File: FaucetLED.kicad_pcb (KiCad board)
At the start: 2 copper layers, 34.5 x 28.4 mm, 43 parts, among them P1 CONN_01X03, P2 CONN_01X02, P4 CONN_01X03, P5 CONN_01X02, P6 CONN_01X01, Q1 BSS138, Q2 BSS138, Q3 BSS138, U1 TLV70033DDC, U2 STM32L052KxTx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

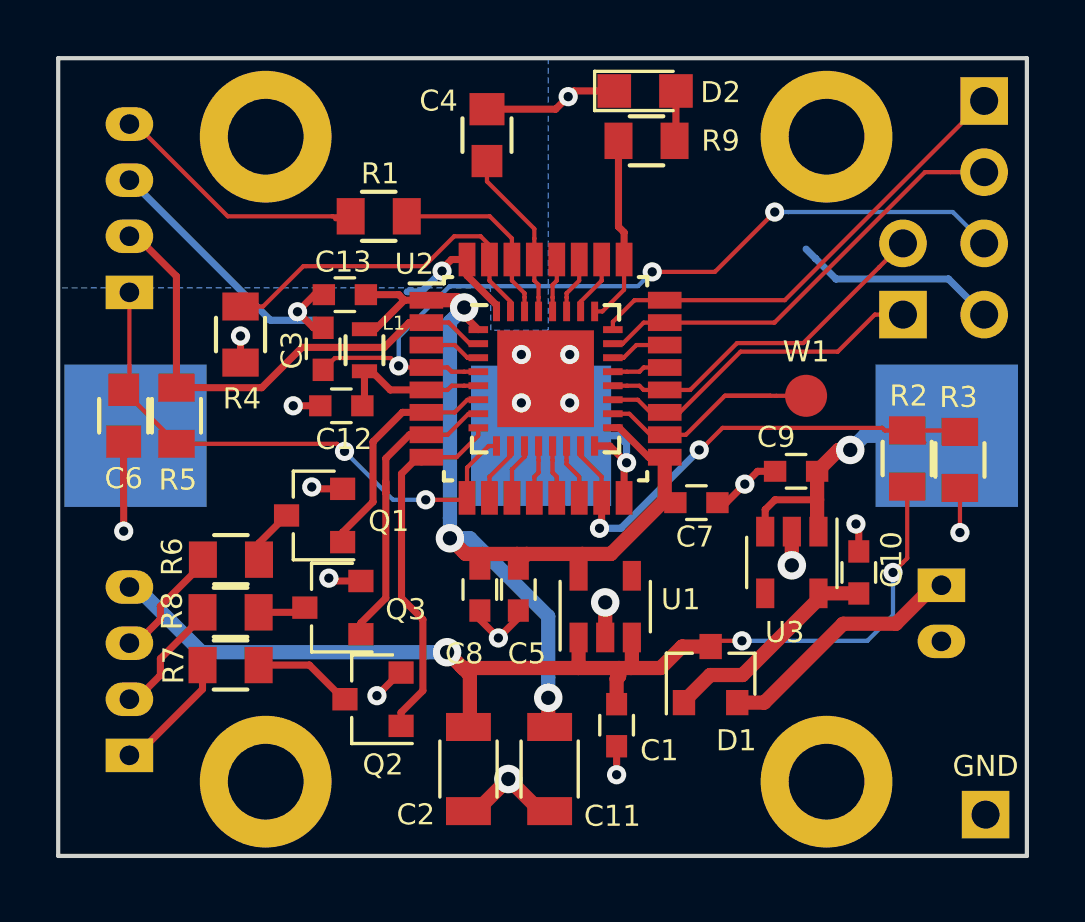
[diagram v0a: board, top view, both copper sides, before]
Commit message: Move 100uF cap to battery input.
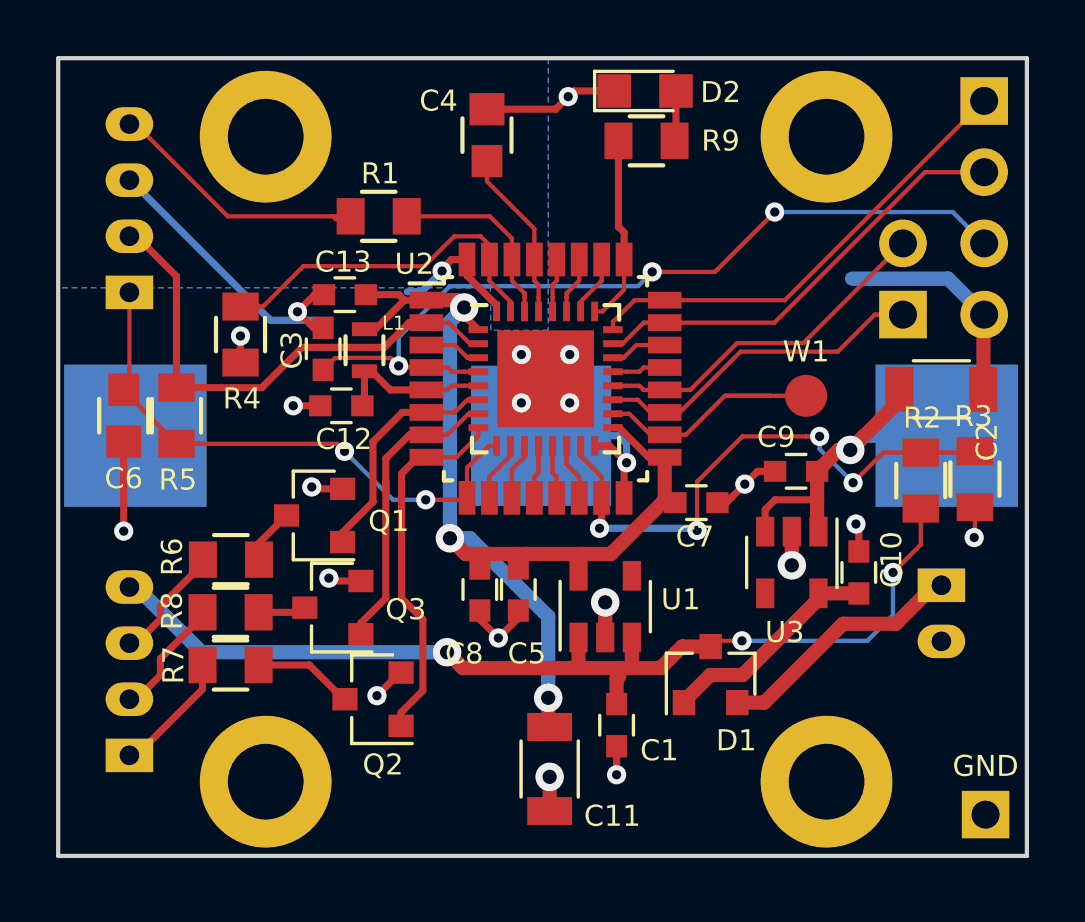
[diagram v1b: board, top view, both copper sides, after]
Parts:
- moved C2 21.6 mm to (133.1, 88.0), turned to 0 degrees
- moved R2 0.92 mm to (132.4, 91.3)
- moved R3 0.87 mm to (134.3, 91.2)
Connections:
- C2 pad 1: +BATT -> Net-(BT1-Pad1)
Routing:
- net Net-(BT1-Pad1): track 10.4 -> 13.3 mm
- net GND: track 65.2 -> 62.7 mm
- net /BATT_2: track 18.6 -> 20.5 mm, vias 2 -> 4
- net +BATT: track 39.9 -> 37.9 mm

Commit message: Move BATT_2 sense R's closer to ADC input.
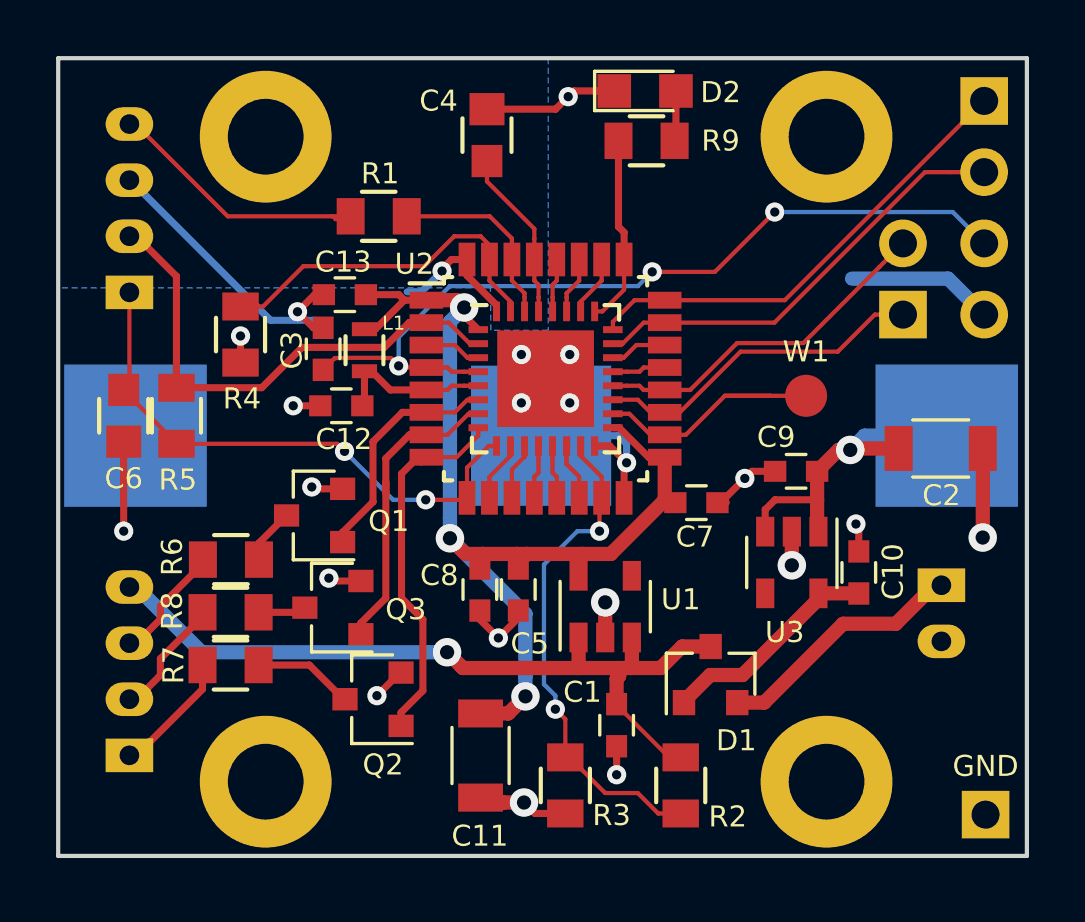
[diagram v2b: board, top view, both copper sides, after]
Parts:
- moved R3 18.2 mm to (119.7, 102.1)
- moved R2 13.8 mm to (123.8, 102.1), turned to 270 degrees
- moved C11 2.51 mm to (116.7, 101.1)
- moved C2 2.11 mm to (133.1, 90.1)
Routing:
- net +BATT: track 37.9 -> 29.4 mm, vias 3 -> 1
- net /BATT_2: track 20.5 -> 18.0 mm, vias 4 -> 2
- net GND: track 62.7 -> 64.5 mm
- net Net-(BT1-Pad1): track 13.3 -> 12.2 mm

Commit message: Add footprint for another bulk cap C14 on +BATT.
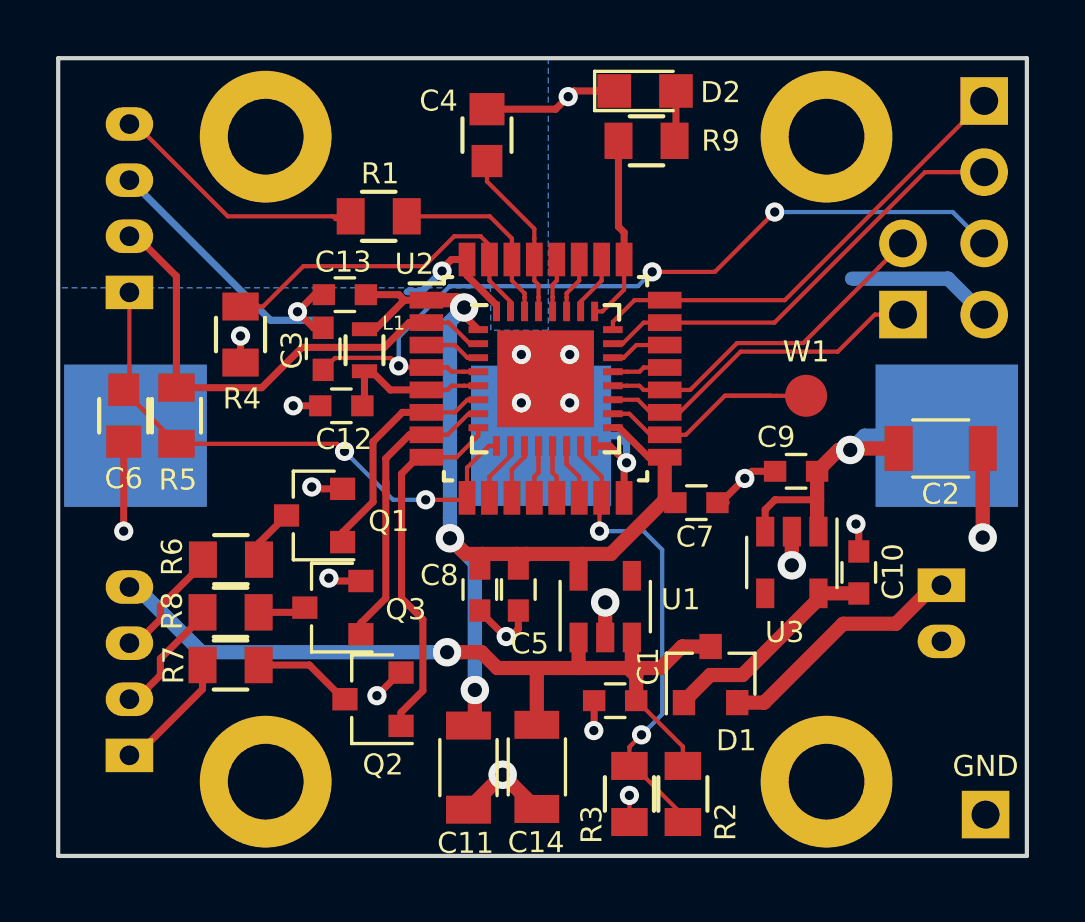
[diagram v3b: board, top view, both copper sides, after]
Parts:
- added C14: 100u, Capacitors_SMD:C_1206, F.Cu at (118.7, 101.5)
- moved R3 2.31 mm to (122.0, 102.4)
- moved C1 0.88 mm to (121.5, 99.1), turned to 180 degrees
- moved C11 0.61 mm to (116.2, 101.5)
- moved R2 0.31 mm to (123.9, 102.4)
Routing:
- net +BATT: track 29.4 -> 31.3 mm
- net +3V3: track 38.6 -> 37.1 mm
- net GND: track 64.5 -> 65.9 mm, vias 22 -> 23
- net /BATT_2: track 18.0 -> 17.0 mm

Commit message: Change C2 and C14 to 1210 package for lower leakage.
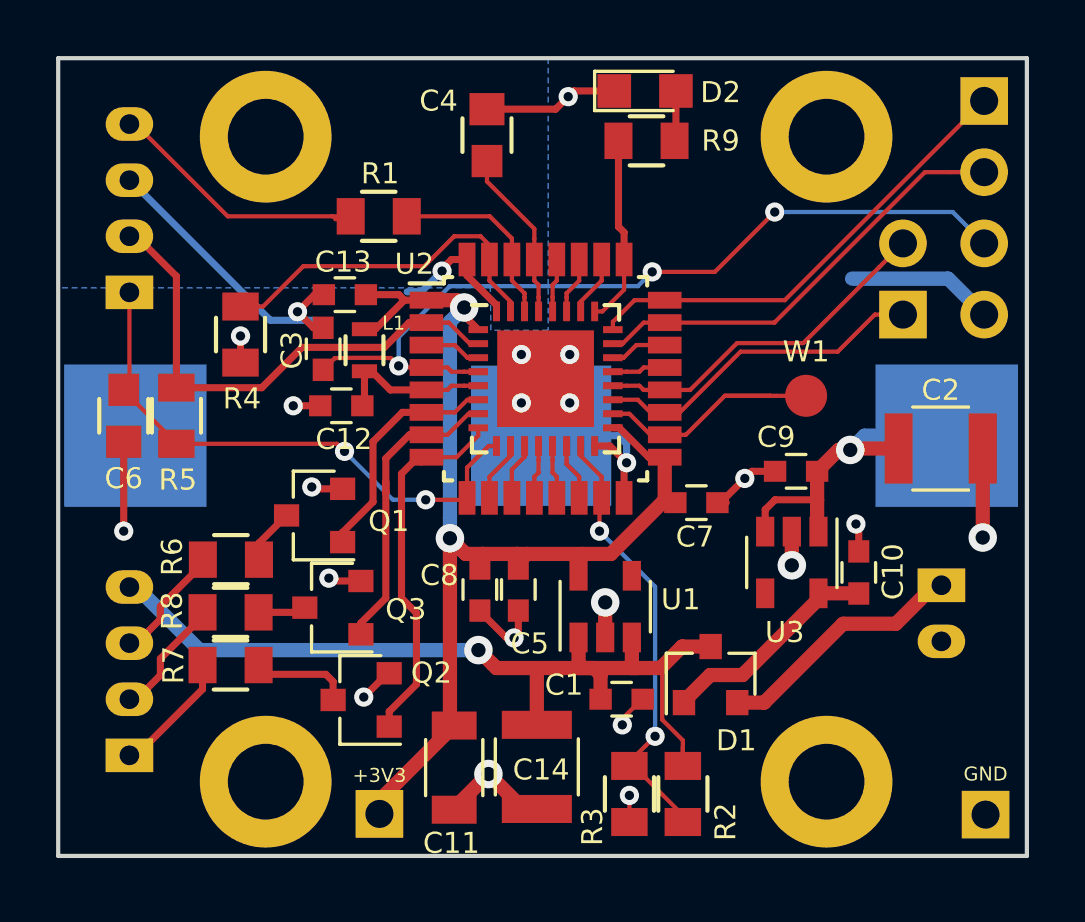
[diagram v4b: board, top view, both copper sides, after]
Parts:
- added P3: CONN_01X01, Pin_Headers:Pin_Header_Straight_1x01_Pitch2.54mm, F.Cu at (113.1, 103.1)
- C14, C2: footprint Capacitors_SMD:C_1206 -> Capacitors_SMD:C_1210
- moved C11 0.51 mm to (115.7, 101.5)
- moved Q2 0.42 mm to (112.4, 99.1)
- moved C1 0.23 mm to (121.7, 99.1), turned to 0 degrees
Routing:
- net +3V3: track 37.1 -> 41.0 mm, vias 3 -> 2
- net +BATT: track 31.3 -> 33.5 mm
- net /BATT_2: track 17.0 -> 15.8 mm
- net GND: track 65.9 -> 66.8 mm
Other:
- board text added: "+3V3"

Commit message: Slight move of C5 closer to 3.3V LDO.
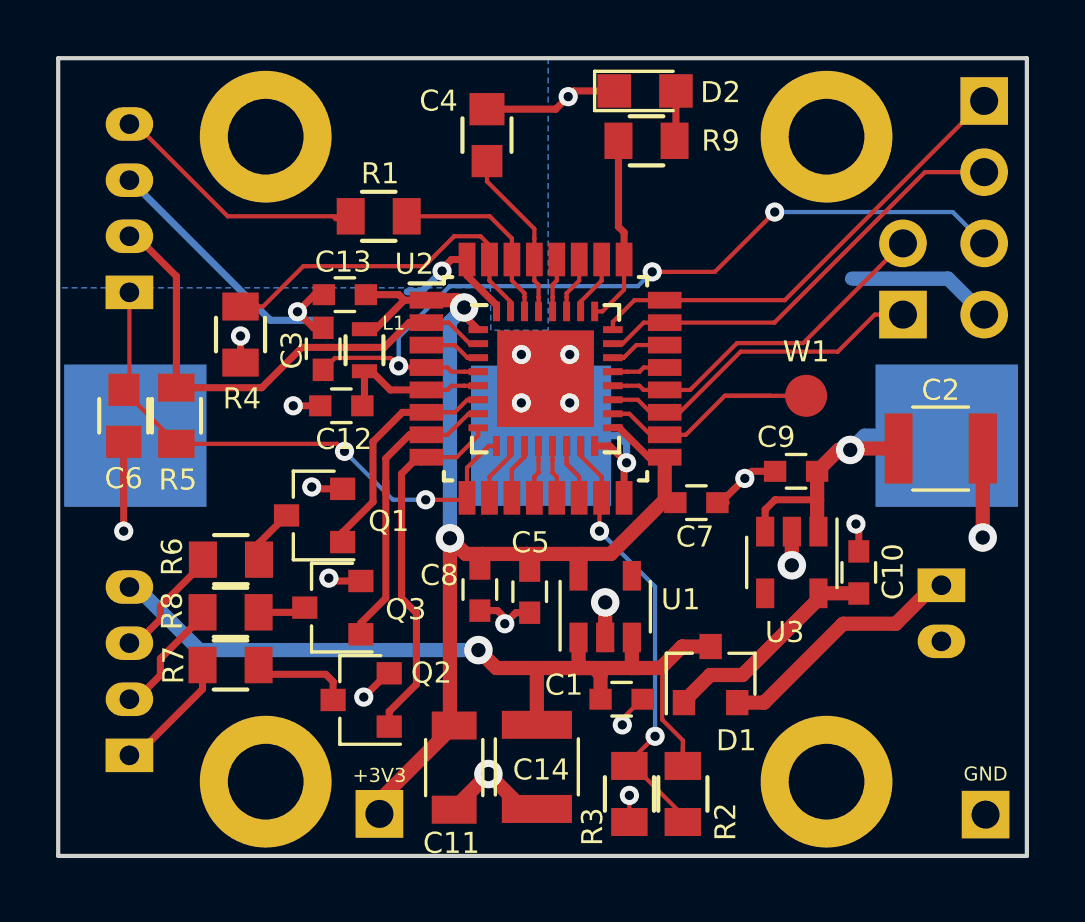
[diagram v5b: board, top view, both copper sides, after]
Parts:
- moved C5 0.41 mm to (118.4, 95.2)
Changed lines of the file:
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@@
     (links 117)
     (no_connects 0)
-    (area 101.524999 76.124999 136.219001 104.723001)
+    (area 96.1526 74.9126 141.1584 106.5668)
     (thickness 1.6)
     (drawings 16)
-    (tracks 452)
+    (tracks 451)
     (zones 0)
     (modules 45)
@@
     (tags "Through hole pin header THT 1x01 2.54mm single row")
     (fp_text reference P3 (at -0.0508 1.8288) (layer F.SilkS) hide
-      (effects (font (size 1 1) (thickness 0.15)))
+      (effects (font (size 0.75 0.75) (thickness 0.12)))
     )
     (fp_text value CONN_01X01 (at 0 2.39) (layer F.Fab)
@@
   )
   (module Capacitors_SMD:C_0603 (layer F.Cu)
-    (at 118.0084 95.1484 270)
+    (at 118.4148 95.2246 270)
     (descr "Capacitor SMD 0603, reflow soldering, AVX (see smccp.pdf)")
     (tags "capacitor 0603")
     (attr smd)
-    (fp_text reference C5 (at 1.9304 -0.4064 360) (layer F.SilkS)
+    (fp_text reference C5 (at -1.7526 -0.0254 360) (layer F.SilkS)
       (effects (font (size 0.75 0.75) (thickness 0.12)))
     )
@@
   (gr_line (start 101.6 104.648) (end 136.144 104.648) (layer Edge.Cuts) (width 0.15))
   (gr_line (start 101.6 76.2) (end 101.6 104.648) (layer Edge.Cuts) (width 0.15))
-  (segment (start 118.0084 96.7232) (end 117.856 96.8756) (width 0.254) (layer F.Cu) (net 1))
-  (segment (start 116.6368 95.9234) (end 117.589 96.8756) (width 0.254) (layer F.Cu) (net 1))
-  (segment (start 116.6368 95.8984) (end 116.6368 95.9234) (width 0.254) (layer F.Cu) (net 1))
-  (segment (start 117.589 96.8756) (end 117.856 96.8756) (width 0.254) (layer F.Cu) (net 1))
-  (segment (start 118.0084 95.8984) (end 118.0084 96.7232) (width 0.254) (layer F.Cu) (net 1))
-  (via (at 117.856 96.8756) (size 0.6858) (drill 0.3302) (layers F.Cu B.Cu) (net 1))
+  (segment (start 118.4148 95.9746) (end 117.9188 95.9746) (width 0.254) (layer F.Cu) (net 1))
+  (segment (start 117.9188 95.9746) (end 117.5258 96.3676) (width 0.254) (layer F.Cu) (net 1))
+  (segment (start 117.5258 96.1584) (end 117.5258 96.3676) (width 0.254) (layer F.Cu) (net 1))
+  (segment (start 117.2658 95.8984) (end 117.5258 96.1584) (width 0.254) (layer F.Cu) (net 1))
+  (segment (start 116.6368 95.8984) (end 117.2658 95.8984) (width 0.254) (layer F.Cu) (net 1))
+  (via (at 117.5258 96.3676) (size 0.6858) (drill 0.3302) (layers F.Cu B.Cu) (net 1))
   (segment (start 113.4044 98.1354) (end 113.345 98.1354) (width 0.254) (layer F.Cu) (net 1))
   (segment (start 113.345 98.1354) (end 112.4966 98.9838) (width 0.254) (layer F.Cu) (net 1))
@@
   (segment (start 111.3536 94.8436) (end 111.252 94.742) (width 0.254) (layer F.Cu) (net 1))
   (via (at 111.252 94.742) (size 0.6858) (drill 0.3302) (layers F.Cu B.Cu) (net 1))
+  (segment (start 118.4148 94.4746) (end 118.4148 93.979996) (width 0.508) (layer F.Cu) (net 2))
+  (segment (start 118.4148 93.979996) (end 118.3132 93.878396) (width 0.508) (layer F.Cu) (net 2))
+  (segment (start 113.0554 102.6654) (end 115.7224 99.9984) (width 0.508) (layer F.Cu) (net 2))
   (segment (start 113.0554 103.1494) (end 113.0554 102.6654) (width 0.508) (layer F.Cu) (net 2))
-  (segment (start 113.0554 102.6654) (end 115.7224 99.9984) (width 0.508) (layer F.Cu) (net 2))
   (segment (start 115.57 93.319596) (end 115.57 99.846) (width 0.508) (layer F.Cu) (net 2))
   (segment (start 115.57 99.846) (end 115.7224 99.9984) (width 0.508) (layer F.Cu) (net 2))
@@
   (segment (start 123.6084 92.0496) (end 123.3208 92.0496) (width 0.508) (layer F.Cu) (net 2))
   (segment (start 123.3208 92.0496) (end 123.23 91.9588) (width 0.508) (layer F.Cu) (net 2))
-  (segment (start 118.0084 94.3984) (end 118.0084 93.929196) (width 0.508) (layer F.Cu) (net 2))
-  (segment (start 118.0084 93.929196) (end 117.9576 93.878396) (width 0.508) (layer F.Cu) (net 2))
   (segment (start 116.6368 94.3984) (end 116.6368 93.979996) (width 0.508) (layer F.Cu) (net 2))
   (segment (start 116.6368 93.979996) (end 116.6876 93.929196) (width 0.508) (layer F.Cu) (net 2))
   (segment (start 120.2944 93.878396) (end 118.3132 93.878396) (width 0.508) (layer F.Cu) (net 2))
   (segment (start 118.3132 93.878396) (end 117.9576 93.878396) (width 0.508) (layer F.Cu) (net 2))
-  (segment (start 118.2116 93.979996) (end 118.3132 93.878396) (width 0.508) (layer F.Cu) (net 2))
   (segment (start 121.310404 93.878396) (end 120.2944 93.878396) (width 0.508) (layer F.Cu) (net 2))
   (segment (start 120.1572 94.658) (end 120.1572 94.015596) (width 0.508) (layer F.Cu) (net 2))

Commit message: Make all 0.1uF caps 100nF, update some notes.
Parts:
- C1, C3, C6, C9: value 0.1u -> 100n
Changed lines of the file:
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@@
   )
   (setup
-    (last_trace_width 0.508)
+    (last_trace_width 0.254)
     (user_trace_width 0.1524)
     (user_trace_width 0.254)
@@
       (effects (font (size 0.75 0.75) (thickness 0.12)))
     )
-    (fp_text value 0.1u (at 0 2.1 270) (layer F.Fab)
+    (fp_text value 100n (at 0 2.1 270) (layer F.Fab)
       (effects (font (size 0.75 0.75) (thickness 0.12)))
     )
@@
       (effects (font (size 0.75 0.75) (thickness 0.12)))
     )
-    (fp_text value 0.1u (at 0 1.5) (layer F.Fab)
+    (fp_text value 100n (at 0 1.5) (layer F.Fab)
       (effects (font (size 0.75 0.75) (thickness 0.12)))
     )
@@
       (effects (font (size 0.75 0.75) (thickness 0.12)))
     )
-    (fp_text value 0.1u (at 0 1.5 180) (layer F.Fab)
+    (fp_text value 100n (at 0 1.5 180) (layer F.Fab)
       (effects (font (size 0.75 0.75) (thickness 0.12)))
     )
@@
       (effects (font (size 0.75 0.75) (thickness 0.12)))
     )
-    (fp_text value 0.1u (at 0 1.5 90) (layer F.Fab)
+    (fp_text value 100n (at 0 1.5 90) (layer F.Fab)
       (effects (font (size 1 1) (thickness 0.15)))
     )

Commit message: C4: Sampling capacitor: Change value to 0.1uF.
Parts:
- C4: value 0.47u -> 0.1u
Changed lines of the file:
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@@
       (effects (font (size 0.75 0.75) (thickness 0.12)))
     )
-    (fp_text value 0.47u (at 0 2.1 90) (layer F.Fab)
+    (fp_text value 0.1u (at 0 2.1 90) (layer F.Fab)
       (effects (font (size 0.75 0.75) (thickness 0.12)))
     )
